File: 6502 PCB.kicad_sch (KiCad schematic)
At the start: 14 parts, among them J1 power_source, J17 Conn_01x16_Pin, SW1 RESET, U1 W65C02S, U2 28C256, U3 62256, U4 W65C22, U5 74HC00, X1 1MHz

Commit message: maybe wrok
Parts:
- added C2, C3: 0.1uf, Capacitor_THT:C_Disc_D4.3mm_W1.9mm_P5.00mm, symbol Device:C
- added J2: Conn_01x02_Pin, Connector_PinHeader_2.00mm:PinHeader_1x02_P2.00mm_Vertical, symbol Connector:Conn_01x02_Pin
- C1: footprint Capacitor_THT:C_Disc_D5.0mm_W2.5mm_P5.00mm -> Capacitor_THT:C_Disc_D4.3mm_W1.9mm_P5.00mm
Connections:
- net GND: now also J2.1 (Pin_1)
- net VDD: now also C2.1, C2.2, C3.1, C3.2, J2.2 (Pin_2)
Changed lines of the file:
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@@
+    (stroke (width 0) (type default))
+  )
+  (wire (pts (xy 215.9 27.94) (xy 219.71 27.94))
     (stroke (width 0) (type default))
   )
@@
   )
   (wire (pts (xy 68.58 26.67) (xy 68.58 16.51))
+    (stroke (width 0) (type default))
+  )
+  (wire (pts (xy 215.9 25.4) (xy 219.71 25.4))
     (stroke (width 0) (type default))
   )
@@
     (effects (font (size 1.27 1.27)) (justify right))
   )
+  (hierarchical_label "VDD" (shape input) (at 19.05 97.79 270) (fields_autoplaced)
+    (effects (font (size 1.27 1.27)) (justify right))
+  )
+  (hierarchical_label "VDD" (shape input) (at 19.05 90.17 90) (fields_autoplaced)
+    (effects (font (size 1.27 1.27)) (justify left))
+  )
   (hierarchical_label "GND" (shape input) (at 57.15 120.65 270) (fields_autoplaced)
     (effects (font (size 1.27 1.27)) (justify right))
   )
+  (hierarchical_label "VDD" (shape input) (at 33.02 90.17 90) (fields_autoplaced)
+    (effects (font (size 1.27 1.27)) (justify left))
+  )
   (hierarchical_label "VDD" (shape input) (at 25.4 19.05 0) (fields_autoplaced)
     (effects (font (size 1.27 1.27)) (justify left))
@@
     (effects (font (size 1.27 1.27)) (justify right))
   )
+  (hierarchical_label "VDD" (shape input) (at 215.9 25.4 180) (fields_autoplaced)
+    (effects (font (size 1.27 1.27)) (justify right))
+  )
   (hierarchical_label "GND" (shape input) (at 199.39 116.84 270) (fields_autoplaced)
     (effects (font (size 1.27 1.27)) (justify right))
@@
     (effects (font (size 1.27 1.27)) (justify right))
   )
+  (hierarchical_label "VDD" (shape input) (at 33.02 97.79 270) (fields_autoplaced)
+    (effects (font (size 1.27 1.27)) (justify right))
+  )
   (hierarchical_label "GND" (shape input) (at 30.48 40.64 270) (fields_autoplaced)
     (effects (font (size 1.27 1.27)) (justify right))
@@
   (hierarchical_label "VDD" (shape input) (at 15.24 25.4 90) (fields_autoplaced)
     (effects (font (size 1.27 1.27)) (justify left))
+  )
+  (hierarchical_label "GND" (shape input) (at 215.9 27.94 180) (fields_autoplaced)
+    (effects (font (size 1.27 1.27)) (justify right))
   )
   (hierarchical_label "VDD" (shape input) (at 199.39 45.72 90) (fields_autoplaced)
@@
     )
   )
+  (symbol (lib_id "Device:C") (at 33.02 93.98 0) (unit 1)
+    (in_bom yes) (on_board yes) (dnp no) (fields_autoplaced)
+    (property "Reference" "C3" (at 36.83 92.71 0)
+      (effects (font (size 1.27 1.27)) (justify left))
+    )
+    (property "Value" "0.1uf" (at 36.83 95.25 0)
+      (effects (font (size 1.27 1.27)) (justify left))
+    )
+    (property "Footprint" "Capacitor_THT:C_Disc_D4.3mm_W1.9mm_P5.00mm" (at 33.9852 97.79 0)
+      (effects (font (size 1.27 1.27)) hide)
+    )
+    (property "Datasheet" "~" (at 33.02 93.98 0)
+      (effects (font (size 1.27 1.27)) hide)
+    )
+    (pin "1")
+    (pin "2")
+    (instances
+      (project "6502 PCB"
+        (path "/28248d1b-65d0-4e2e-a100-551a14ee840a"
+          (reference "C3") (unit 1)
+        )
+      )
+    )
+  )
   (symbol (lib_id "Switch:SW_Push") (at 26.67 33.02 270) (unit 1)
     (in_bom yes) (on_board yes) (dnp no)
@@
         (path "/28248d1b-65d0-4e2e-a100-551a14ee840a"
           (reference "SW1") (unit 1)
+        )
+      )
+    )
+  )
+  (symbol (lib_id "Connector:Conn_01x02_Pin") (at 224.79 27.94 180) (unit 1)
+    (in_bom yes) (on_board yes) (dnp no) (fields_autoplaced)
+    (property "Reference" "J2" (at 226.06 25.4 0)
+      (effects (font (size 1.27 1.27)) (justify right))
+    )
+    (property "Value" "Conn_01x02_Pin" (at 226.06 27.94 0)
+      (effects (font (size 1.27 1.27)) (justify right))
+    )
+    (property "Footprint" "Connector_PinHeader_2.00mm:PinHeader_1x02_P2.00mm_Vertical" (at 224.79 27.94 0)
+      (effects (font (size 1.27 1.27)) hide)
+    )
+    (property "Datasheet" "~" (at 224.79 27.94 0)
+      (effects (font (size 1.27 1.27)) hide)
+    )
+    (pin "1")
+    (pin "2")
+    (instances
+      (project "6502 PCB"
+        (path "/28248d1b-65d0-4e2e-a100-551a14ee840a"
+          (reference "J2") (unit 1)
         )
       )
@@
       (effects (font (size 1.27 1.27)) (justify left))
     )
-    (property "Footprint" "Capacitor_THT:C_Disc_D5.0mm_W2.5mm_P5.00mm" (at 35.2552 36.83 0)
+    (property "Footprint" "Capacitor_THT:C_Disc_D4.3mm_W1.9mm_P5.00mm" (at 35.2552 36.83 0)
       (effects (font (size 1.27 1.27)) hide)
     )
@@
         )
       )
+    )
+  )
+  (symbol (lib_id "Device:C") (at 19.05 93.98 0) (unit 1)
+    (in_bom yes) (on_board yes) (dnp no) (fields_autoplaced)
+    (property "Reference" "C2" (at 22.86 92.71 0)
+      (effects (font (size 1.27 1.27)) (justify left))
+    )
+    (property "Value" "0.1uf" (at 22.86 95.25 0)
+      (effects (font (size 1.27 1.27)) (justify left))
+    )
+    (property "Footprint" "Capacitor_THT:C_Disc_D4.3mm_W1.9mm_P5.00mm" (at 20.0152 97.79 0)
+      (effects (font (size 1.27 1.27)) hide)
+    )
+    (property "Datasheet" "~" (at 19.05 93.98 0)
+      (effects (font (size 1.27 1.27)) hide)
+    )
+    (pin "1")
+    (pin "2")
+    (instances
+      (project "6502 PCB"
+        (path "/28248d1b-65d0-4e2e-a100-551a14ee840a"
+          (reference "C2") (unit 1)
+        )
+      )

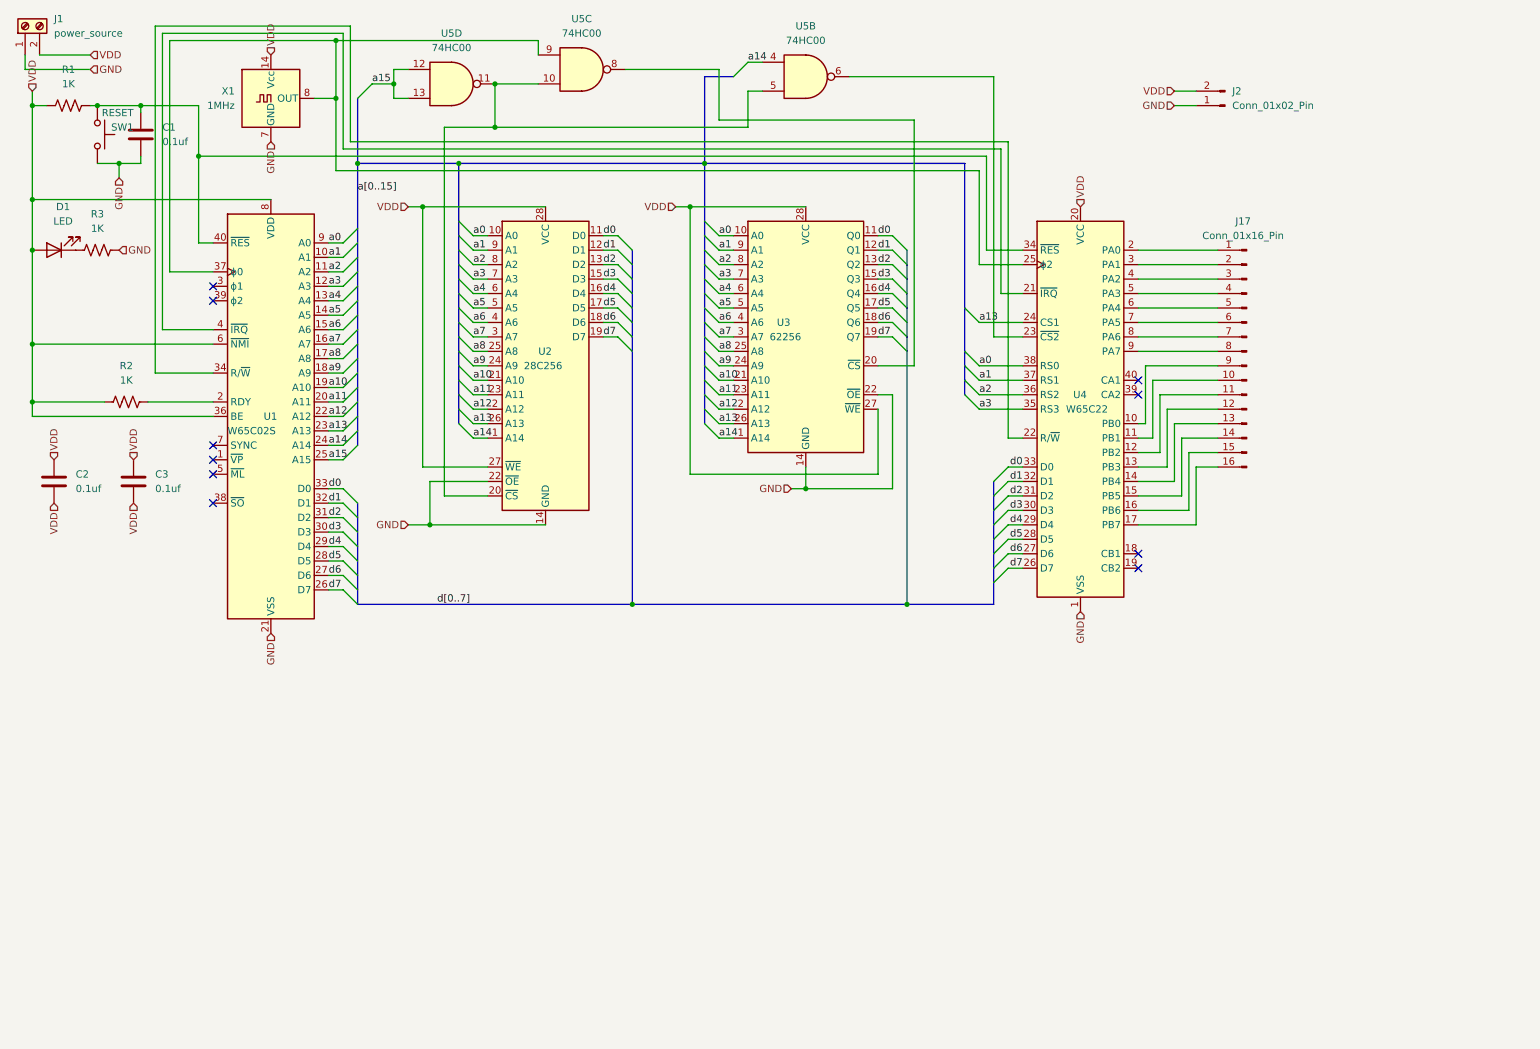
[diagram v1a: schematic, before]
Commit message: changed schematic
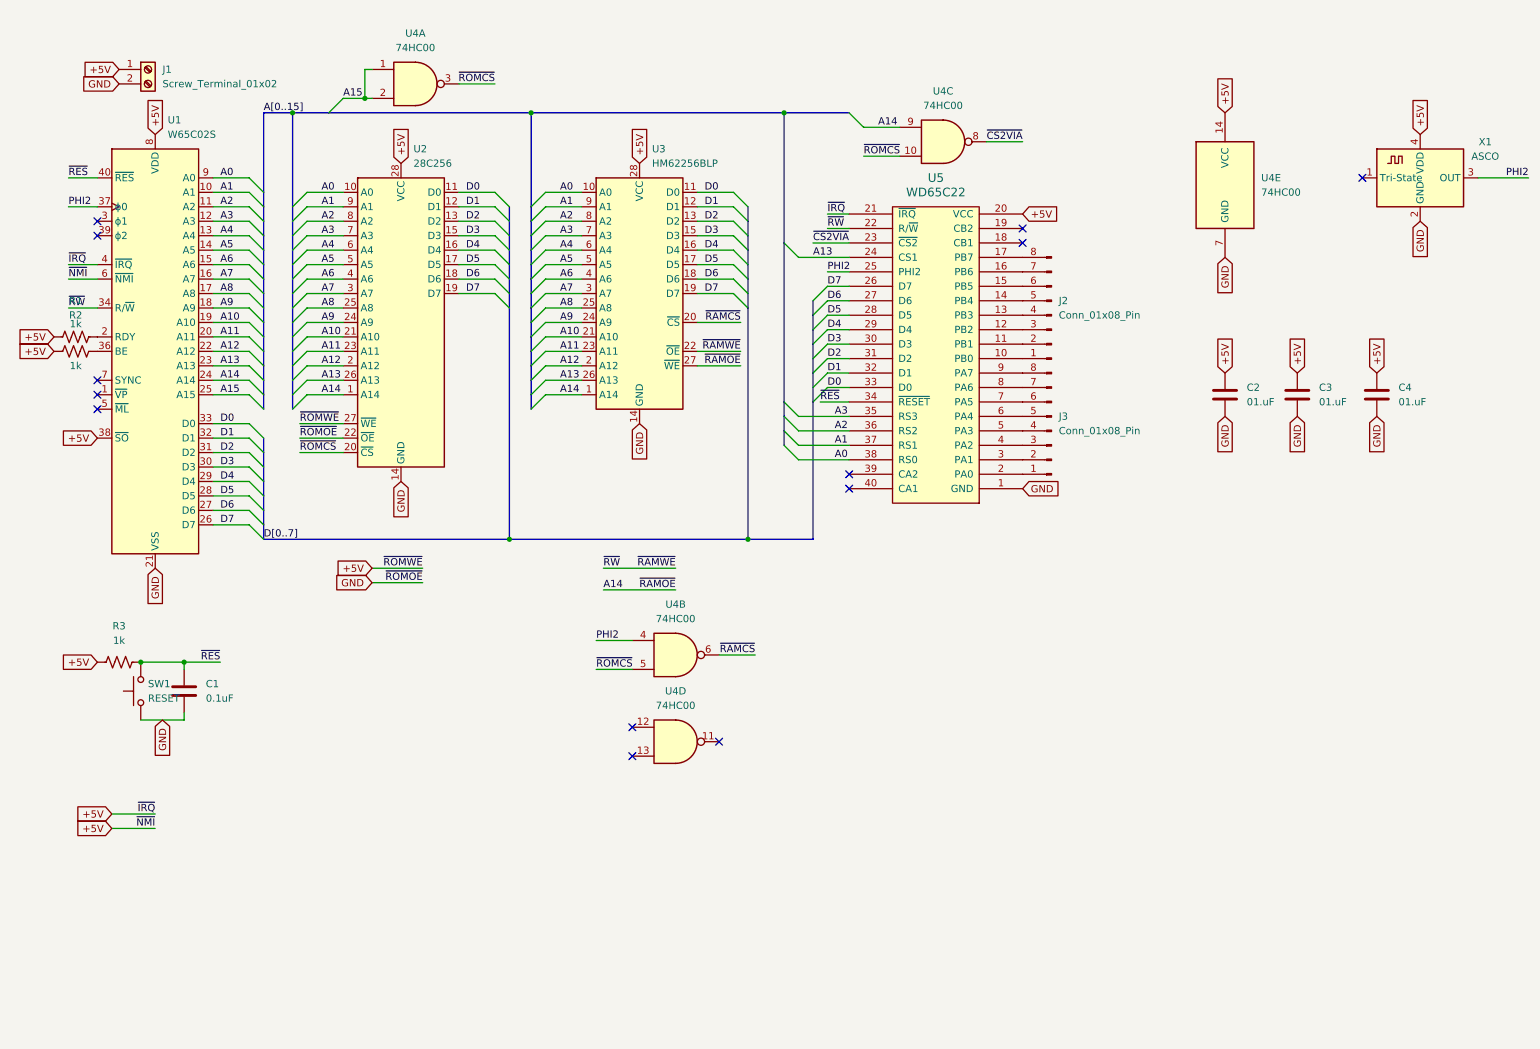
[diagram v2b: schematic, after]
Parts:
- removed D1: LED, LED_THT:LED_D3.0mm, symbol Device:LED
- removed J17: Conn_01x16_Pin, Connector_PinHeader_2.00mm:PinHeader_1x16_P2.00mm_Vertical, symbol Connector:Conn_01x16_Pin
- removed J2: Conn_01x02_Pin, Connector_PinHeader_2.00mm:PinHeader_1x02_P2.00mm_Vertical, symbol Connector:Conn_01x02_Pin
- removed U1: W65C02S, Package_DIP:DIP-40_W15.24mm, symbol 65xx-library:W65C02SxP
- removed U3: 62256, Package_DIP:DIP-28_W15.24mm, symbol Memory_RAM:CY62256-70PC
- removed U4: W65C22, Package_DIP:DIP-40_W15.24mm, symbol 65xx-library:W65C22NxP
- removed U5: 74HC00, Package_DIP:DIP-14_W7.62mm, symbol 74xx:74HC00
- removed X1: 1MHz, Oscillator:Oscillator_DIP-14, symbol Oscillator:ACO-xxxMHz
- added C4: 01.uF, symbol Device:C
- added J2, J3: Conn_01x08_Pin, symbol Connector:Conn_01x08_Pin
- added U1: W65C02S, Package_DIP:DIP-40_W15.24mm, symbol W65C02S:W65C02S
- added U3: HM62256BLP, Package_DIP:DIP-28_W15.24mm, symbol Memory_RAM:HM62256BLP
- added U4: 74HC00, symbol 74xx:74HC00
- added U5: WD65C22, symbol 65xx:WD65C22
- added X1: ASCO, Oscillator:Oscillator_SMD_Abracon_ASCO-4Pin_1.6x1.2mm, symbol Oscillator:ASCO
- C1: value 0.1uf -> 0.1uF; footprint Capacitor_THT:C_Disc_D4.3mm_W1.9mm_P5.00mm -> (none)
- C2, C3: value 0.1uf -> 01.uF; footprint Capacitor_THT:C_Disc_D4.3mm_W1.9mm_P5.00mm -> (none)
- J1: value power_source -> Screw_Terminal_01x02; footprint TerminalBlock:TerminalBlock_bornier-2_P5.08mm -> (none)
- R1, R2, R3: value 1K -> 1k; footprint Resistor_THT:R_Axial_DIN0204_L3.6mm_D1.6mm_P7.62mm_Horizontal -> (none)
- SW1: footprint Button_Switch_THT:SW_PUSH_6mm -> (none)
- U2: footprint Package_DIP:DIP-28_W15.24mm -> (none)
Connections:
- net GND: now also C2.2, C3.2, J1.2 (Pin_2), SW1.1, C4.2, U1.21 (VSS), U3.14 (GND), U4.7 (GND), U5.1 (GND), X1.2 (GND); no longer J1.1 (Pin_1), R3.2, SW1.2
- net ~{ROMCS}: now reaches U2.20 (~{CS})
- net ~{ROMCS}: now also U4.10, U4.3, U4.5
- net +5V: now reaches R3.1
- net +5V: now also C2.1, C3.1, J1.1 (Pin_1), R1.1, R2.1, U2.27 (~{WE}), U2.28 (VCC), C4.1, U1.38 (~{SO}), U1.4 (~{IRQ}), U1.6 (~{NMI}), U1.8 (VDD), U3.28 (VCC), U4.14 (VCC), U5.20 (VCC), U5.21 (~{IRQ}), X1.4 (VDD)
- net at R2.2: now also U1.36 (BE)
- removed net VDD: C2.1, C2.2, C3.1, C3.2, J1.2 (Pin_2), R1.1, R2.1, U2.27 (~{WE}), U2.28 (VCC)
- net a0 renamed A0
- net A0: now also U1.9 (A0), U3.10 (A0), U5.38 (RS0)
- net a1 renamed A1
- net A1: now also U1.10 (A1), U3.9 (A1), U5.37 (RS1)
- net a10 renamed A10
- net A10: now also U1.19 (A10), U3.21 (A10)
- net a11 renamed A11
- net A11: now also U1.20 (A11), U3.23 (A11)
- net a12 renamed A12
- net A12: now also U1.22 (A12), U3.2 (A12)
- net a13 renamed A13
- net A13: now also U1.23 (A13), U3.26 (A13), U5.24 (CS1)
- net a14 renamed A14
- net A14: now also U1.24 (A14), U3.1 (A14), U3.27 (~{WE}), U4.9
- net a2 renamed A2
- net A2: now also U1.11 (A2), U3.8 (A2), U5.36 (RS2)
- net a3 renamed A3
- net A3: now also U1.12 (A3), U3.7 (A3), U5.35 (RS3)
- net a4 renamed A4
- net A4: now also U1.13 (A4), U3.6 (A4)
- net a5 renamed A5
- net A5: now also U1.14 (A5), U3.5 (A5)
- net a6 renamed A6
- net A6: now also U1.15 (A6), U3.4 (A6)
- net a7 renamed A7
- net A7: now also U1.16 (A7), U3.3 (A7)
- net a8 renamed A8
- net A8: now also U1.17 (A8), U3.25 (A8)
- net a9 renamed A9
- net A9: now also U1.18 (A9), U3.24 (A9)
- net d0 renamed D0
- net D0: now also U1.33 (D0), U3.11 (D0), U5.33 (D0)
- net d1 renamed D1
- net D1: now also U1.32 (D1), U3.12 (D1), U5.32 (D1)
- net d2 renamed D2
- net D2: now also U1.31 (D2), U3.13 (D2), U5.31 (D2)
- net d3 renamed D3
- net D3: now also U1.30 (D3), U3.15 (D3), U5.30 (D3)
- net d4 renamed D4
- net D4: now also U1.29 (D4), U3.16 (D4), U5.29 (D4)
- net d5 renamed D5
- net D5: now also U1.28 (D5), U3.17 (D5), U5.28 (D5)
- net d6 renamed D6
- net D6: now also U1.27 (D6), U3.18 (D6), U5.27 (D6)
- net d7 renamed D7
- net D7: now also U1.26 (D7), U3.19 (D7), U5.26 (D7)
- new net: J3.1 (Pin_1), U5.2 (PA0)
- new net: J3.2 (Pin_2), U5.3 (PA1)
- new net: J3.3 (Pin_3), U5.4 (PA2)
- new net: J3.4 (Pin_4), U5.5 (PA3)
- new net: J3.5 (Pin_5), U5.6 (PA4)
- new net: J3.6 (Pin_6), U5.7 (PA5)
- new net: J3.7 (Pin_7), U5.8 (PA6)
- new net: J3.8 (Pin_8), U5.9 (PA7)
- new net: J2.1 (Pin_1), U5.10 (PB0)
- new net: J2.2 (Pin_2), U5.11 (PB1)
- new net: J2.3 (Pin_3), U5.12 (PB2)
- new net: J2.4 (Pin_4), U5.13 (PB3)
- new net: J2.5 (Pin_5), U5.14 (PB4)
- new net: J2.6 (Pin_6), U5.15 (PB5)
- new net: J2.7 (Pin_7), U5.16 (PB6)
- new net: J2.8 (Pin_8), U5.17 (PB7)
- new net: R1.2, U1.2 (RDY)
- new net A15: U1.25 (A15), U4.1, U4.2
- new net PHI2: U1.37 (ϕ0), U4.4, U5.25 (PHI2), X1.3 (OUT)
- new net ~{CS2VIA}: U4.8, U5.23 (~{CS2})
- new net ~{RAMCS}: U3.20 (~{CS}), U4.6
- new net ~{RAMWE}: U1.34 (R/~{W}), U3.22 (~{OE}), U5.22 (R/~{W})
- new net ~{RES}: C1.1, R3.2, SW1.2, U1.40 (~{RES}), U5.34 (~{RESET})
- no-connect marks 10 -> 13

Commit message: aaaa
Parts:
- removed J2, J3: Conn_01x08_Pin, symbol Connector:Conn_01x08_Pin
- removed X1: ASCO, Oscillator:Oscillator_SMD_Abracon_ASCO-4Pin_1.6x1.2mm, symbol Oscillator:ASCO
- added D1: LED, LED_THT:LED_D5.0mm, symbol Device:LED
- added J2: Conn_01x16_Pin, Connector_PinSocket_2.54mm:PinSocket_1x16_P2.54mm_Vertical, symbol Connector:Conn_01x16_Pin
- added R4: 3.3k, Resistor_THT:R_Axial_DIN0207_L6.3mm_D2.5mm_P7.62mm_Horizontal, symbol Device:R_US
- added X1: 1MHz, Oscillator:Oscillator_DIP-14, symbol Oscillator:ACO-xxxMHz
- C1, C2, C3, C4: footprint (none) -> Capacitor_THT:C_Disc_D3.0mm_W1.6mm_P2.50mm
- J1: footprint (none) -> TerminalBlock:TerminalBlock_bornier-2_P5.08mm
- R1, R2, R3: footprint (none) -> Resistor_THT:R_Axial_DIN0207_L6.3mm_D2.5mm_P7.62mm_Horizontal
- SW1: footprint (none) -> Button_Switch_THT:SW_PUSH_6mm
- U2: footprint (none) -> Package_DIP:DIP-28_W15.24mm
- U4: footprint (none) -> Package_DIP:DIP-14_W7.62mm
- U5: footprint (none) -> Package_DIP:DIP-40_W15.24mm
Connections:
- net +5V: now also D1.2 (A), X1.14 (Vcc)
- net GND: now also R4.2, X1.7 (GND)
- net PHI2: now also X1.8 (OUT)
- net at U5.2 (PA0): now also J2.1 (Pin_1)
- net at U5.3 (PA1): now also J2.2 (Pin_2)
- net at U5.4 (PA2): now also J2.3 (Pin_3)
- net at U5.5 (PA3): now also J2.4 (Pin_4)
- net at U5.6 (PA4): now also J2.5 (Pin_5)
- net at U5.7 (PA5): now also J2.6 (Pin_6)
- net at U5.8 (PA6): now also J2.7 (Pin_7)
- net at U5.9 (PA7): now also J2.8 (Pin_8)
- net at U5.10 (PB0): now also J2.9 (Pin_9)
- net at U5.11 (PB1): now also J2.10 (Pin_10)
- net at U5.12 (PB2): now also J2.11 (Pin_11)
- net at U5.13 (PB3): now also J2.12 (Pin_12)
- net at U5.14 (PB4): now also J2.13 (Pin_13)
- net at U5.15 (PB5): now also J2.14 (Pin_14)
- net at U5.16 (PB6): now also J2.15 (Pin_15)
- net at U5.17 (PB7): now also J2.16 (Pin_16)
- new net: D1.1 (K), R4.1
- no-connect marks 13 -> 12
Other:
- moved on the sheet: U4D
